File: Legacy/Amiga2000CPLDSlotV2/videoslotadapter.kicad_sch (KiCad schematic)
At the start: 20 parts, among them J1 Raspberry_Pi_2_3, SW1 Select, SW2 Down, SW3 Up, U1 XC9572VQ44

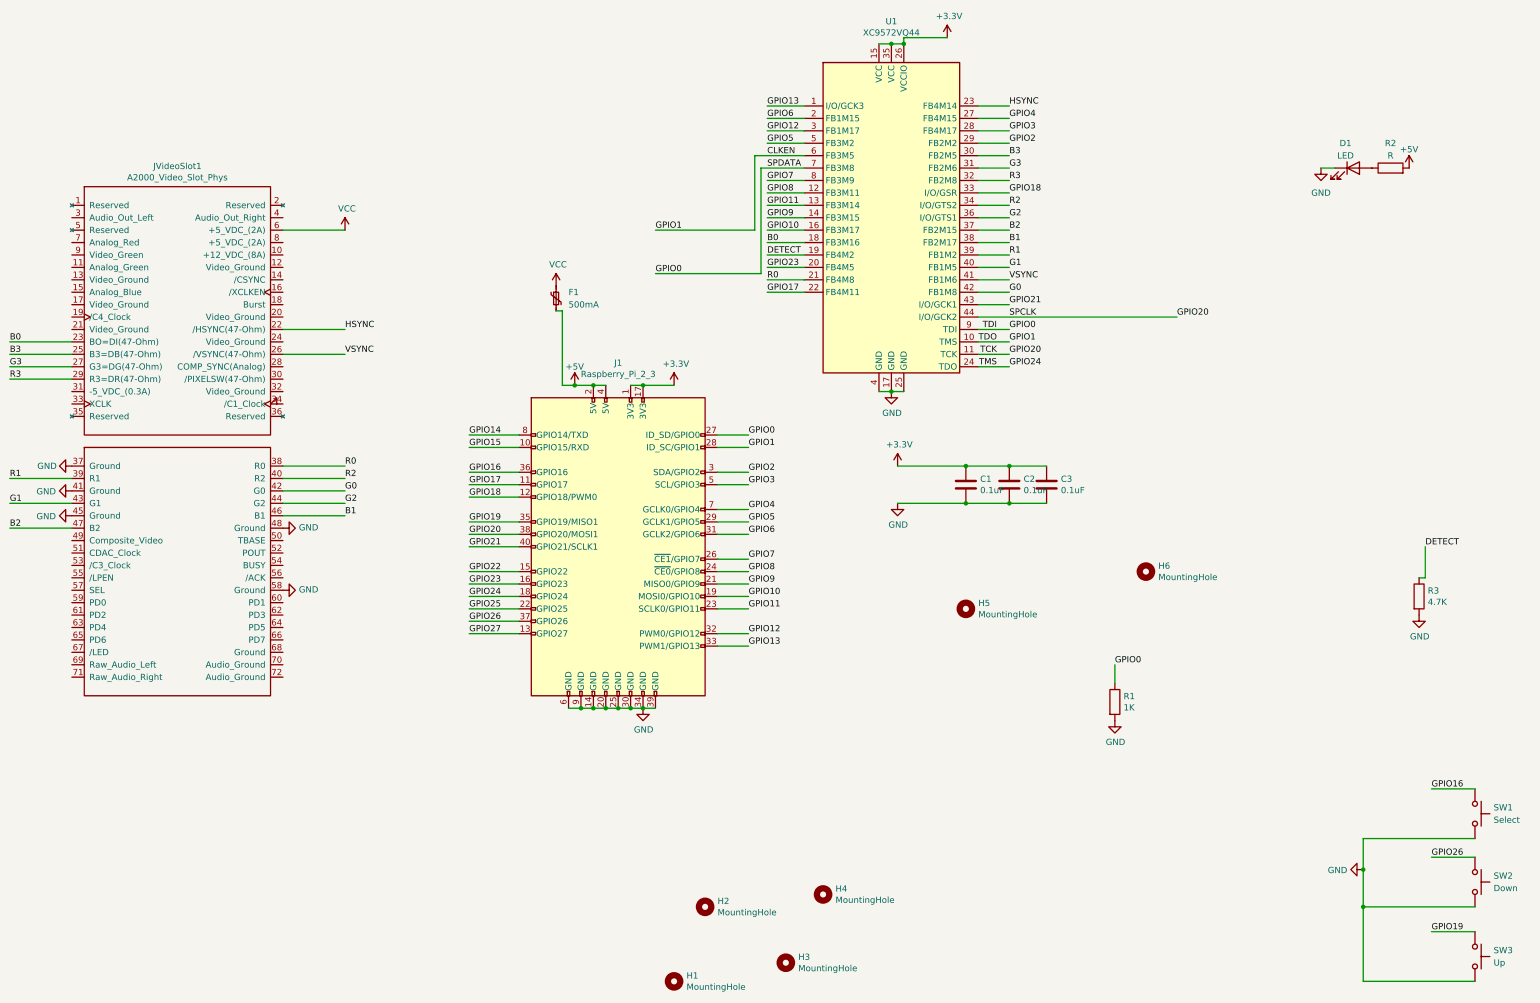
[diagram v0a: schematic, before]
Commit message: Add Amiga 2000 RGBtoHDMI v2.2
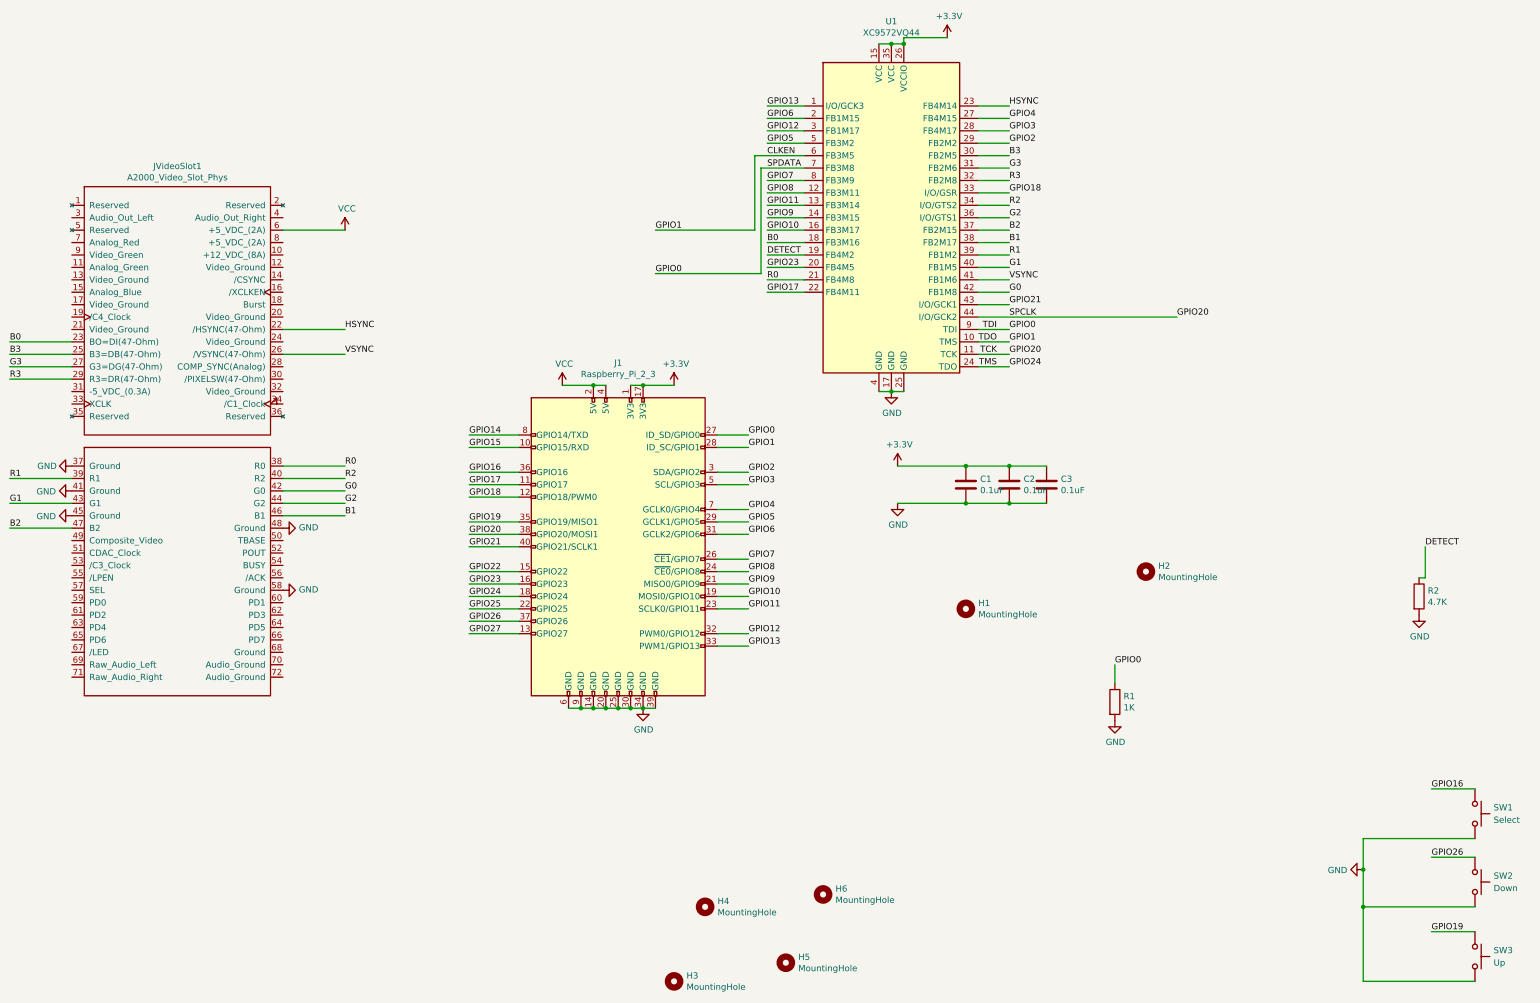
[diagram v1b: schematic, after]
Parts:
- removed D1: LED, Diode_SMD_Handsoldering_AKL:D_0603_1608Metric_Pad1.05x0.95mm, symbol Device:LED
- removed F1: 500mA, Fuse_Handsoldering_AKL:Fuse_1206_3216Metric_Pad1.42x1.75mm_BigPads, symbol Device:Polyfuse_Small
- removed R2: R, Resistor_SMD_AKL:R_0603_1608Metric_Pad1.05x0.95mm_HandSolder, symbol Device:R
- C1, C2, C3: footprint Capacitor_SMD_Handsoldering_AKL:C_0603_1608Metric_Pad1.08x0.95mm -> Capacitor_SMD:C_0603_1608Metric_Pad1.08x0.95mm_HandSolder
- H1: renamed from H5; footprint MountingHole:MountingHole_3.2mm_M3_Pad_Via -> MountingHole:MountingHole_3.2mm_M3
- H2: renamed from H6; footprint MountingHole:MountingHole_3.2mm_M3_Pad_Via -> MountingHole:MountingHole_3.2mm_M3
- H3: renamed from H1; footprint MountingHole:MountingHole_2.7mm_M2.5_Pad_Via -> MountingHole:MountingHole_2.7mm_M2.5
- H4: renamed from H2; footprint MountingHole:MountingHole_2.7mm_M2.5_Pad_Via -> MountingHole:MountingHole_2.7mm_M2.5
- H5: renamed from H3; footprint MountingHole:MountingHole_2.7mm_M2.5_Pad_Via -> MountingHole:MountingHole_2.7mm_M2.5
- H6: renamed from H4; footprint MountingHole:MountingHole_2.7mm_M2.5_Pad_Via -> MountingHole:MountingHole_2.7mm_M2.5
- R1: footprint Resistor_SMD_AKL:R_0603_1608Metric_Pad1.05x0.95mm_HandSolder -> Resistor_SMD:R_0603_1608Metric_Pad0.98x0.95mm_HandSolder
- R2: renamed from R3; footprint Resistor_SMD_AKL:R_0603_1608Metric_Pad1.05x0.95mm_HandSolder -> Resistor_SMD:R_0603_1608Metric_Pad0.98x0.95mm_HandSolder
- U1: footprint Package_QFP_AKL:TQFP-44_10x10mm_P0.8mm -> Package_QFP:TQFP-44_10x10mm_P0.8mm
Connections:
- net +5V is gone; now on net VCC: J1.2 (5V), J1.4 (5V)
